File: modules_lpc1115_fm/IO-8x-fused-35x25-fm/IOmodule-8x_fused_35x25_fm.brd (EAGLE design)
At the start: 35 x 25 mm, 86 parts, among them IC1 LPC1115, IC2 ATAES132A-SHEQ-T, Q2 ASFL, U1 EEPROM, X3 MICROMATCH-10

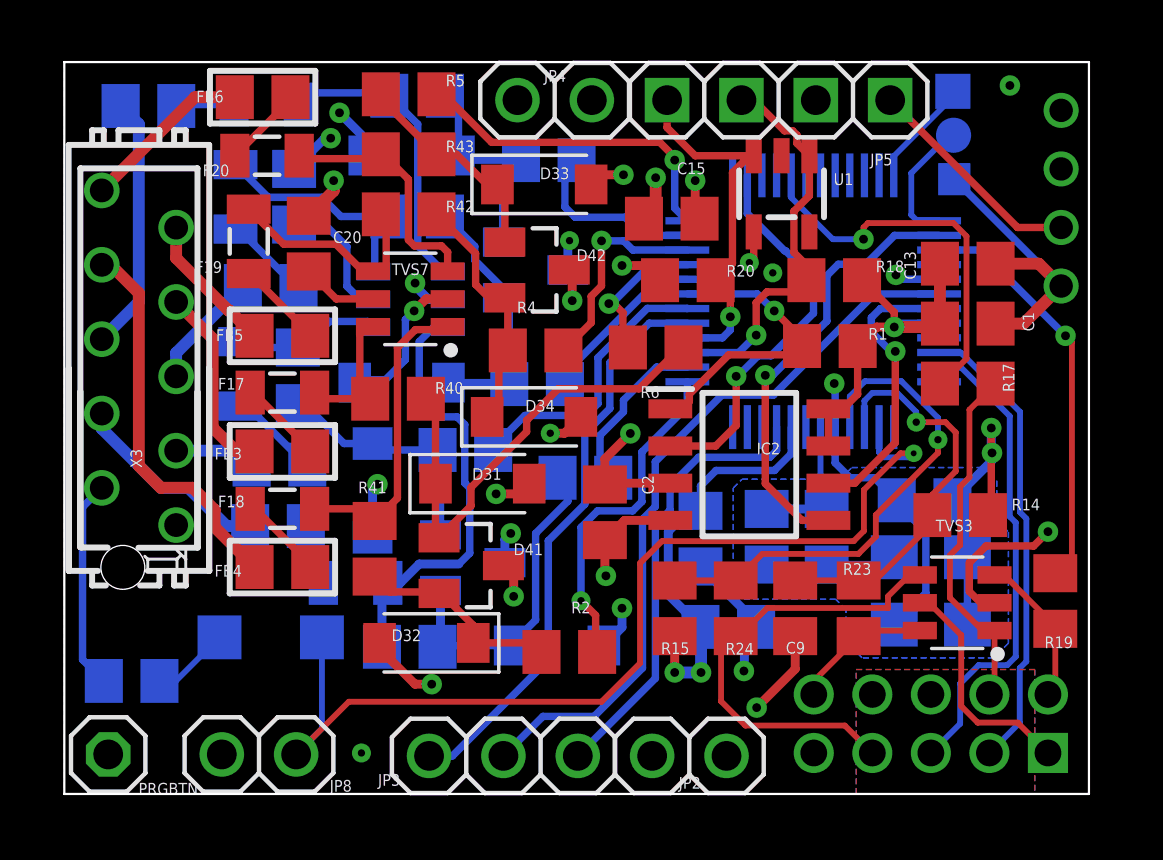
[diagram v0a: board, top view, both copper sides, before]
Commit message: [IOmodule8xFM] parts re-arranged; pin assignement of I2C conn. corrected
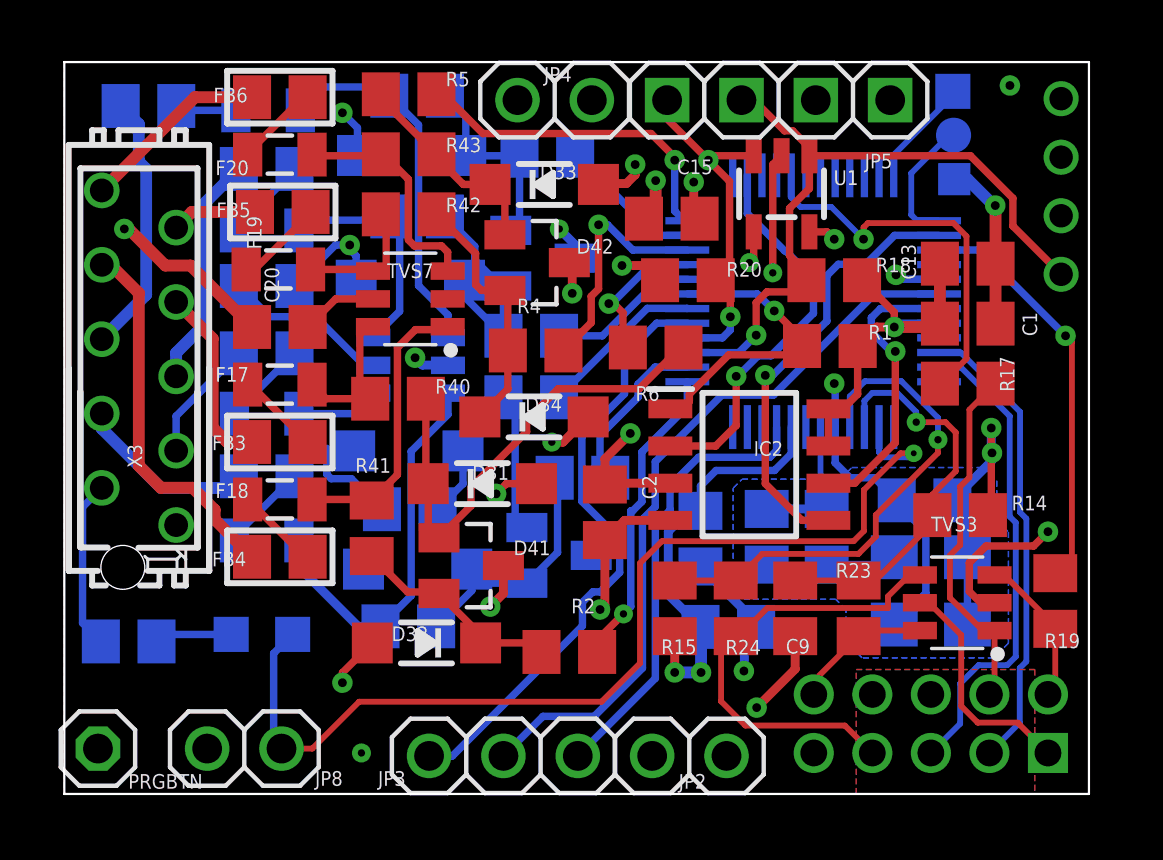
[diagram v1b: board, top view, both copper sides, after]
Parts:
- D31: device Diode:SODFL3718X115 -> microbuilder:SOD-123
- D32, D33, D35, D36, D37, D38: value DIODE -> DDZ9684; device Diode:SODFL3718X115 -> microbuilder:SOD-123
- D34: value PDZ3.3BGWJ -> DDZ9684; device Diode:SODFL3718X115 -> microbuilder:SOD-123
- F17, F18, F19, F20, F21, F22, F23: value 0805L035 -> BSMD0805-005-33V
- F24: value 0805L050 -> BSMD0805-005-33V
- LED1: device led:CHIPLED_1206 -> led:CHIPLED_0805
- moved R44 5.96 mm to (11.8, 9.72), turned to 180 degrees
- moved D38 5.43 mm to (12.1, 7.68), turned to 0 degrees
- moved FB5 4.23 mm to (7.46, 19.9)
- moved FB8 4.00 mm to (6.91, 21.4)
- moved FB10 3.83 mm to (6.91, 15.1)
- moved D35 3.51 mm to (11.8, 17.6)
- moved F22 3.37 mm to (6.91, 8.66)
- moved C21 3.19 mm to (6.91, 17.4), turned to 0 degrees
- moved C20 3.02 mm to (7.36, 15.9), turned to 0 degrees
- moved D40 2.96 mm to (16.9, 8.15)
- moved R9 2.88 mm to (15.9, 13.6)
- moved TVS8 2.25 mm to (11.8, 14.6)
- moved D37 1.83 mm to (11.8, 11.7), turned to 0 degrees
- moved FB9 1.74 mm to (6.91, 10.8)
- moved R7 1.66 mm to (15.9, 15.7)
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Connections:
- net +3V3: now also JP1.3; no longer JP1.2
- net GND: now also D31.A, D32.A, D33.A, D34.A, D35.A, D36.A, D37.A, D38.A, JP1.4; no longer D31.2, D32.2, D33.2, D34.2, D35.2, D36.2, D37.2, D38.2, JP1.1
- net IO1R: now also D37.C; no longer D37.1
- net IO2R: now also D38.C; no longer D38.1
- net IO3R: now also D35.C; no longer D35.1
- net IO4R: now also D36.C; no longer D36.1
- net IO5R: now also D31.C; no longer D31.1
- net IO6R: now also D32.C; no longer D32.1
- net IO7R: now also D34.C; no longer D34.1
- net IO8R: now also D33.C; no longer D33.1
- net SCL: now also JP1.1; no longer JP1.4
- net SDA: now also JP1.2; no longer JP1.3
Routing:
- net +3V3: track 73.0 -> 63.5 mm, vias 13 -> 12
- net IO1: track 9.61 -> 5.66 mm
- net IN3: track 4.03 -> 7.97 mm
- net N$15: track 7.53 -> 4.57 mm
- net IO2R: track 11.2 -> 8.62 mm
- net N$16: track 10.2 -> 12.7 mm
- net IN6: track 4.82 -> 2.91 mm
- net SDA: track 27.1 -> 25.4 mm, vias 1 -> 2
- net N$9: track 15.1 -> 13.5 mm
- net IO4: track 6.41 -> 4.96 mm
- net IN1: track 2.78 -> 4.21 mm
- net SCL: track 25.9 -> 24.6 mm
- net N$18: track 5.08 -> 6.33 mm
- net IO1R: track 8.38 -> 9.54 mm
- net N$48: track 4.56 -> 5.71 mm
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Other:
- board text added: "IO module fused 8x v1.0.0 rc1"
- board text removed: "IO module fused 8x v1.0.0 beta2"

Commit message: [IOmodule8xFM] - switched RX / TX to 2,54 pin header added status LED
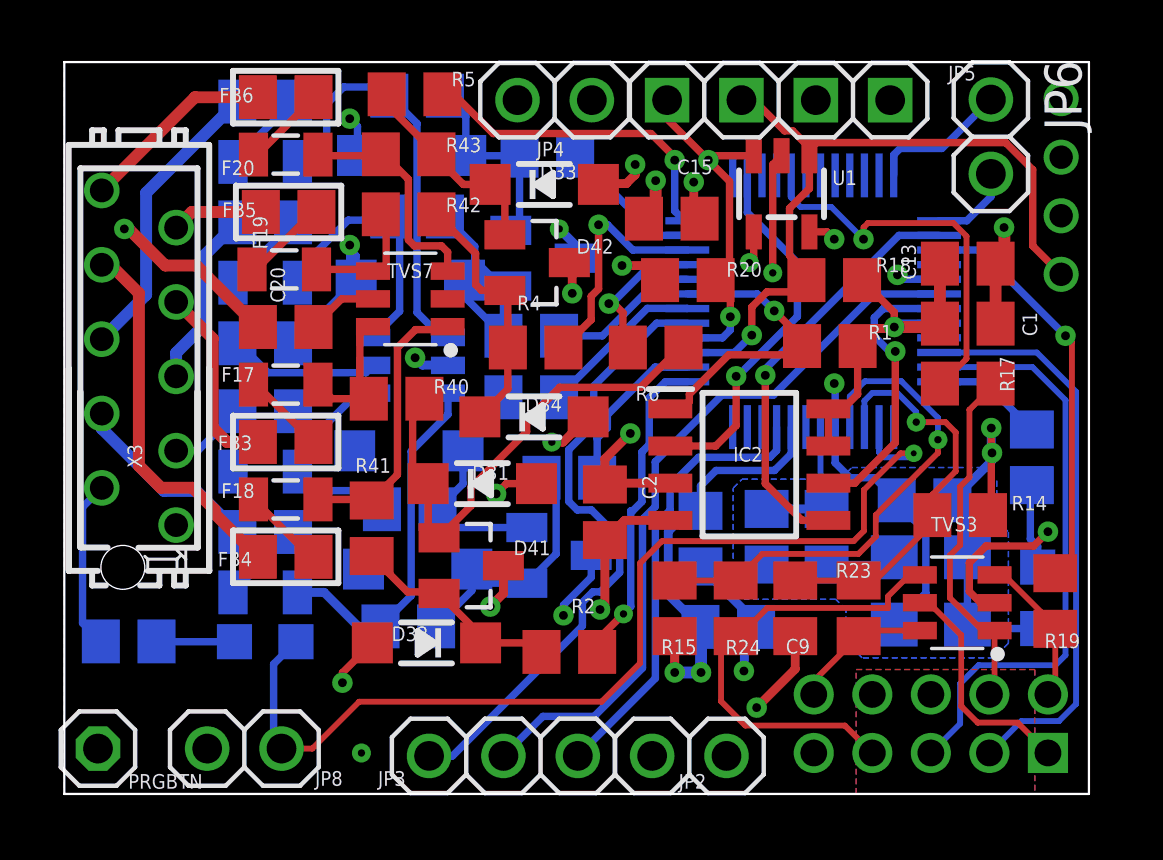
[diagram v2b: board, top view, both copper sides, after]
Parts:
- removed GND: TPTP11SQ, testpad:TP11SQ
- removed RXD: TPTP12R, testpad:TP12R
- removed TXD: TPTP12SQ, testpad:TP12SQ
- added JP6: (no value), pinhead_dmx:1X02
- added LED2: (no value), led:CHIPLED_0805
- added R10: 1k, rcl:R0805
- moved FB7 3.99 mm to (6.86, 23.6)
- moved F21 1.98 mm to (6.86, 11.0)
- moved FB10 1.98 mm to (6.86, 13.1)
- moved C21 1.96 mm to (6.86, 15.4)
- moved FB9 1.90 mm to (6.86, 8.95)
- moved FB8 1.83 mm to (6.86, 19.5)
- moved F23 1.79 mm to (6.86, 17.5)
- moved F22 1.77 mm to (6.86, 6.89)
- moved F24 1.77 mm to (6.86, 21.6)
- moved R3 0.45 mm to (17.2, 10.8)
- moved LED1 0.27 mm to (6.86, 5.20)
- moved R5 0.20 mm to (12.0, 23.9)
- moved C20 0.20 mm to (7.56, 15.9)
- moved F17 0.20 mm to (7.56, 14.0)
- moved F18 0.20 mm to (7.56, 10.1)
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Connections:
- new net N$14: LED2.C, R10.2
- new net N$19: IC1.48, R10.1
- net +3V3: now also LED2.A
- net DBG_RXD: now also JP6.2; no longer RXD.TP
- net DBG_TXD: now also JP6.1; no longer TXD.TP
- net GND: no longer GND.TP
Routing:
- net +3V3: track 63.5 -> 68.5 mm, vias 12 -> 13
- net N$19: track 0.00 -> 3.84 mm
- net ISP_TXD: track 16.5 -> 20.3 mm
- net ISP_RXD: track 15.9 -> 19.6 mm
- net N$14: track 0.00 -> 2.93 mm
- net IN3: track 7.97 -> 6.13 mm
- net N$16: track 12.7 -> 14.3 mm
- net IN1: track 4.21 -> 2.65 mm
- net DBG_RXD: track 4.44 -> 2.89 mm
- net IO1R: track 9.54 -> 8.07 mm
- net SCL: track 24.6 -> 26.0 mm
- net N$18: track 6.33 -> 7.58 mm
- net N$9: track 13.5 -> 12.2 mm
- net DBG_TXD: track 3.71 -> 4.80 mm
- net IN4: track 8.95 -> 10.0 mm
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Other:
- board text added: "IO module fused 8x v1.0.0 rc3"
- board text removed: "IO module fused 8x v1.0.0 rc1"

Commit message: [IOmodule8xFM] - moved MLCC to avoid collision with EIB pin of power PCB
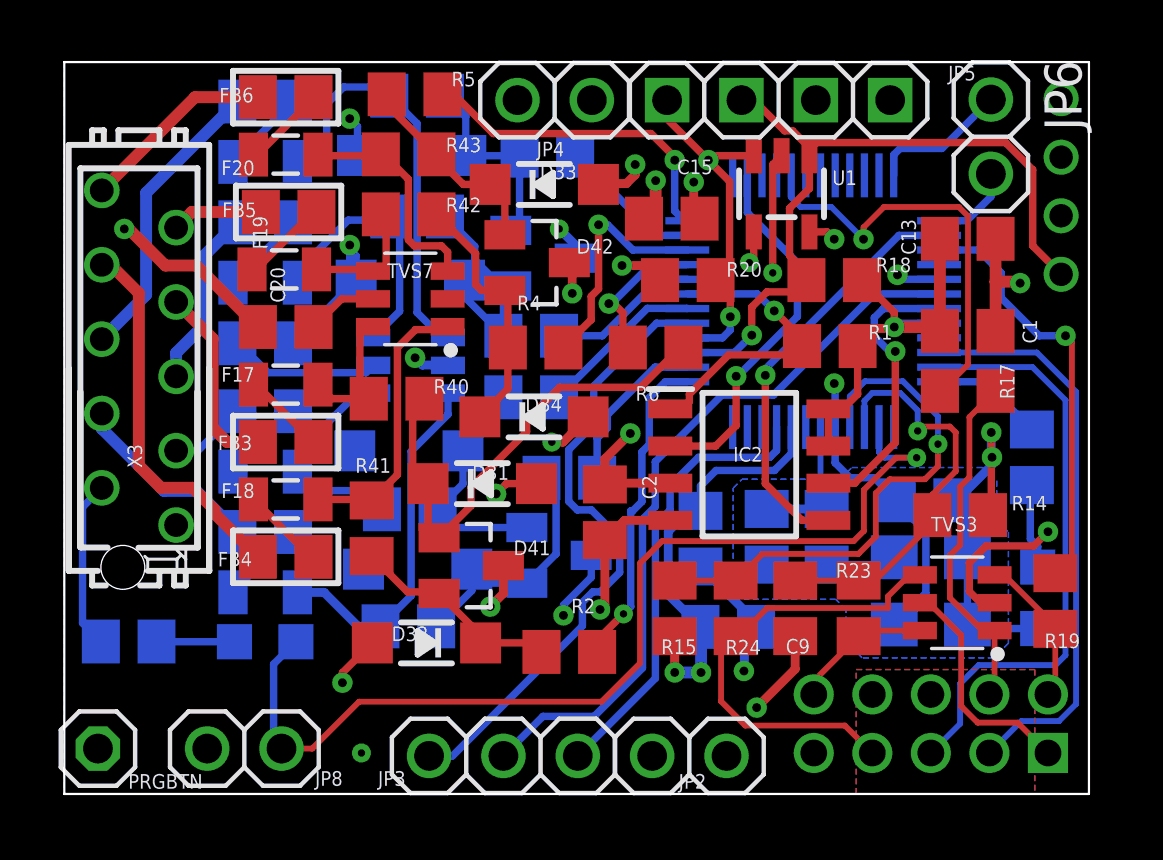
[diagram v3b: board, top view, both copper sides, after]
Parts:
- moved C13 0.85 mm to (30.9, 19.0)
- moved C1 0.25 mm to (30.9, 15.8)
- moved R17 0.25 mm to (30.9, 13.8)
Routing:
- net SWCLK: track 13.4 -> 14.6 mm
- net GND: track 60.2 -> 61.3 mm
- net +3V3: track 68.5 -> 69.4 mm
- net ISP_EN: track 17.2 -> 18.0 mm
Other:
- board text removed: "IO module 8x fused in-wall 35x25 v1.0.0"
